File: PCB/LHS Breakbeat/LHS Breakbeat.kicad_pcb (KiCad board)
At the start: 2 copper layers, 114 x 61.4 mm, 47 parts, among them J1 Steppers In, J10 RGB, J11 Filament Sensor / Tach, J12 Endstop X, J13 Endstop Y, J14 Fan Aux, J15 Fan Part, J16 Fan Hotend/Can HL, J17 Motor X, J19 Motor X1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

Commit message: v1.01: changing copper weight to 2oz, adding xt30 cutout, various tolerance updates
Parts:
- moved TP1 0.20 mm to (160.7, 91.4)
- moved TP2 0.19 mm to (160.8, 94.8)
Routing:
- net /AGND: track 228.3 -> 268.7 mm
- net /X-B1: track 62.0 -> 64.9 mm
- net /X-B2: track 64.7 -> 67.6 mm
- net /Y1-A2: track 54.6 -> 52.3 mm
- net /PWM_HB: track 29.8 -> 28.1 mm
- net /X-A2: track 67.5 -> 66.2 mm
- net /X-A1: track 70.6 -> 69.6 mm
- net GND: track 24.3 -> 25.0 mm
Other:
- outline, holes or cut-outs redrawn
- board text added: "Circuit Limits:"
- board text added: "Gnd⏚"
- board text added: "Hotend Heater: 24V, 115W, 4.8A Bed Heater: 24V, 220W, 9.2A Fans: 24V, 2A RGB/5V: 2A Steppers: 2.7A"
- board text added: "RGB"
- board text added: "VOL 1.01"
- board text added: "⏚"
- board text removed: "Gnd"
- board text removed: "VOL 1"

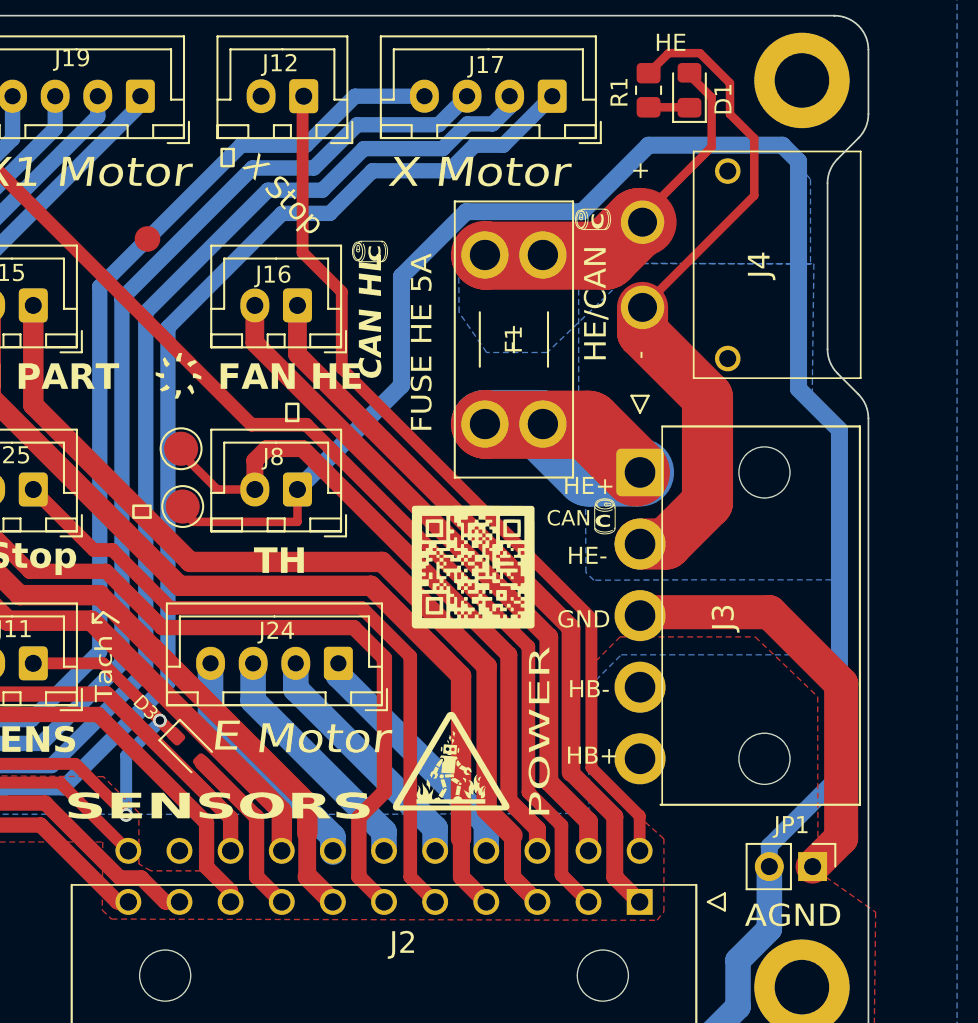
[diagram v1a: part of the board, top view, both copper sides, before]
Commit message: updating zone names
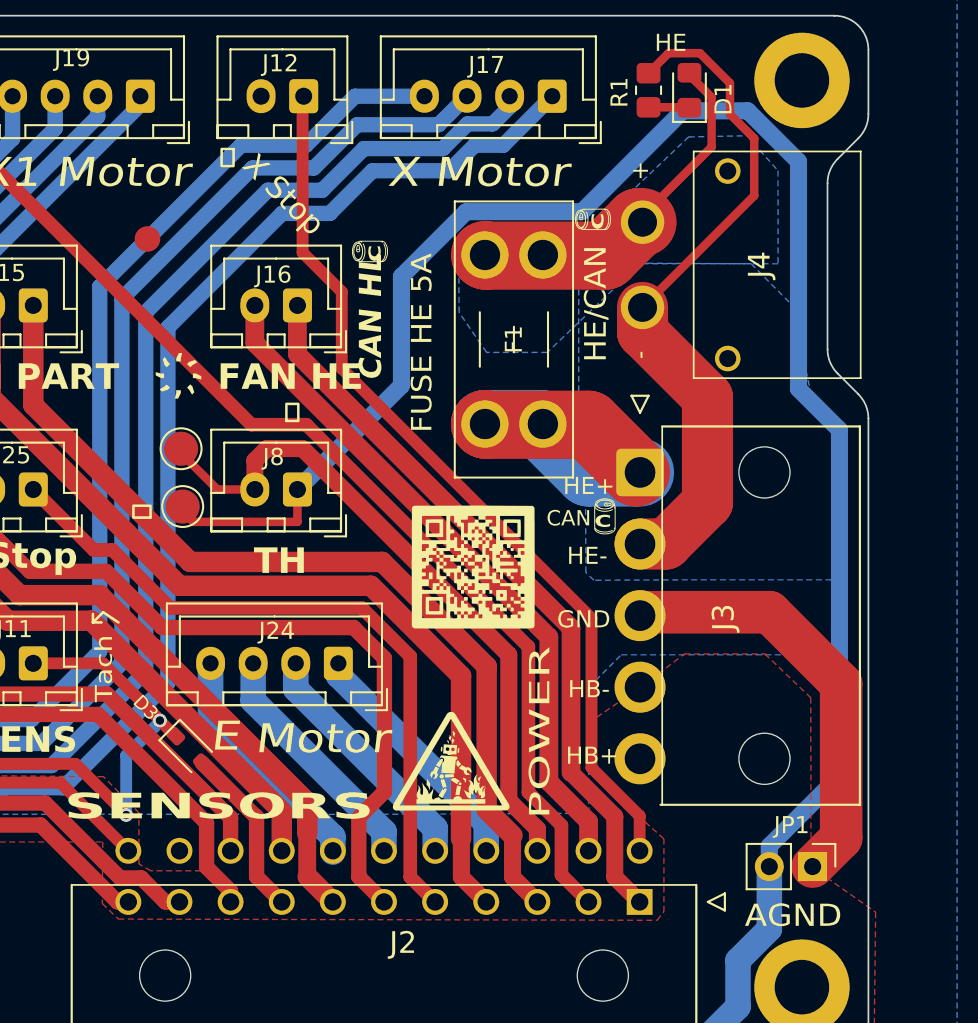
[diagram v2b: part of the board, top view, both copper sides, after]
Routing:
- net /AGND: track 268.7 -> 270.4 mm
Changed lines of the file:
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@@
     (effects (font (size 1 1) (thickness 0.15)))
   )
-  (segment (start 199.4 105.2) (end 199.4 114.25) (width 2) (layer "F.Cu") (net 1))
-  (segment (start 187.8 101) (end 195.2 101) (width 2) (layer "F.Cu") (net 1))
-  (segment (start 199.4 114.25) (end 197.725 115.925) (width 2) (layer "F.Cu") (net 1))
-  (segment (start 187.6 101.2) (end 187.8 101) (width 2) (layer "F.Cu") (net 1))
-  (segment (start 195.2 101) (end 199.4 105.2) (width 2) (layer "F.Cu") (net 1))
+  (segment (start 199.4 105.2) (end 199.4 114.25) (width 2.5) (layer "F.Cu") (net 1))
+  (segment (start 187.8 101) (end 195.2 101) (width 2.5) (layer "F.Cu") (net 1))
+  (segment (start 199.4 114.25) (end 197.725 115.925) (width 2.5) (layer "F.Cu") (net 1))
+  (segment (start 187.6 101.2) (end 187.8 101) (width 2.5) (layer "F.Cu") (net 1))
+  (segment (start 195.2 101) (end 199.4 105.2) (width 2.5) (layer "F.Cu") (net 1))
   (segment (start 190.475 71.375) (end 190.5 71.4) (width 0.25) (layer "F.Cu") (net 2))
   (segment (start 188.1 71.375) (end 190.475 71.375) (width 0.5) (layer "F.Cu") (net 2))
@@
   (segment (start 117.2 90.2) (end 119.1 92.1) (width 1) (layer "F.Cu") (net 10))
   (segment (start 97.2 100.1) (end 95.7 100.1) (width 0.8) (layer "F.Cu") (net 10))
+  (segment (start 177.4 77.5) (end 184.2 77.5) (width 1) (layer "B.Cu") (net 10))
+  (segment (start 196.9 74.56) (end 196.9 87.9) (width 1) (layer "B.Cu") (net 10))
+  (segment (start 193.35 121.425) (end 193.35 124.15) (width 1.5) (layer "B.Cu") (net 10))
   (segment (start 196.9 87.9) (end 199.3 90.3) (width 1) (layer "B.Cu") (net 10))
-  (segment (start 193.35 121.425) (end 193.35 124.15) (width 1.5) (layer "B.Cu") (net 10))
+  (segment (start 167.5 93.8) (end 173.6 87.7) (width 1) (layer "B.Cu") (net 10))
   (segment (start 193.35 124.15) (end 191.05 126.45) (width 1.5) (layer "B.Cu") (net 10))
-  (segment (start 199.3 110.607919) (end 195.185 114.722919) (width 1) (layer "B.Cu") (net 10))
+  (segment (start 184.2 77.5) (end 190.12 71.58) (width 1) (layer "B.Cu") (net 10))
   (segment (start 94.629364 112.229364) (end 94.629364 104.429364) (width 1.5) (layer "B.Cu") (net 10))
   (segment (start 191.05 126.45) (end 111.95 126.45) (width 1.5) (layer "B.Cu") (net 10))
-  (segment (start 167.5 93.8) (end 173.6 87.7) (width 1) (layer "B.Cu") (net 10))
   (segment (start 199.3 90.3) (end 199.3 110.607919) (width 1) (layer "B.Cu") (net 10))
+  (segment (start 173.6 87.7) (end 173.6 81.3) (width 1) (layer "B.Cu") (net 10))
+  (segment (start 193.92 71.58) (end 196.9 74.56) (width 1) (layer "B.Cu") (net 10))
   (segment (start 173.6 81.3) (end 177.4 77.5) (width 1) (layer "B.Cu") (net 10))
-  (segment (start 195.950252 73.6) (end 196.9 74.549748) (width 1) (layer "B.Cu") (net 10))
-  (segment (start 184.2 77.5) (end 188.1 73.6) (width 1) (layer "B.Cu") (net 10))
-  (segment (start 188.1 73.6) (end 195.950252 73.6) (width 1) (layer "B.Cu") (net 10))
-  (segment (start 196.9 74.549748) (end 196.9 87.9) (width 1) (layer "B.Cu") (net 10))
-  (segment (start 173.6 87.7) (end 173.6 81.3) (width 1) (layer "B.Cu") (net 10))
-  (segment (start 195.185 114.722919) (end 195.185 115.925) (width 1) (layer "B.Cu") (net 10))
-  (segment (start 177.4 77.5) (end 184.2 77.5) (width 1) (layer "B.Cu") (net 10))
   (segment (start 111.95 126.45) (end 110.5 125) (width 1.5) (layer "B.Cu") (net 10))
   (segment (start 110.5 125) (end 110.5 122.225) (width 1.5) (layer "B.Cu") (net 10))
+  (segment (start 190.12 71.58) (end 193.92 71.58) (width 1) (layer "B.Cu") (net 10))
+  (segment (start 195.185 114.722919) (end 195.185 115.925) (width 1) (layer "B.Cu") (net 10))
   (segment (start 106.075 117.8) (end 100.2 117.8) (width 1.5) (layer "B.Cu") (net 10))
   (segment (start 195.185 115.925) (end 195.185 119.59) (width 1.5) (layer "B.Cu") (net 10))
@@
   (segment (start 94.629364 104.429364) (end 93 102.8) (width 1.5) (layer "B.Cu") (net 10))
   (segment (start 100.2 117.8) (end 94.629364 112.229364) (width 1.5) (layer "B.Cu") (net 10))
+  (segment (start 199.3 110.607919) (end 195.185 114.722919) (width 1) (layer "B.Cu") (net 10))
   (segment (start 187.57825 112.954848) (end 184.75 110.126598) (width 0.7) (layer "F.Cu") (net 11))
   (segment (start 170.1 82.2) (end 167.8 79.9) (width 0.7) (layer "F.Cu") (net 11))
@@
   (segment (start 187.6 97) (end 189.120279 97) (width 3) (layer "F.Cu") (net 57))
   (segment (start 192.875 69.960051) (end 192.875 71.775) (width 0.5) (layer "F.Cu") (net 57))
-  (zone (net 5) (net_name "+5V") (layer "F.Cu") (name "PWM HB") (hatch edge 0.5)
+  (zone (net 5) (net_name "+5V") (layer "F.Cu") (name "+5V") (hatch edge 0.5)
     (connect_pads yes (clearance 0.4))
     (min_thickness 0.25) (filled_areas_thickness no)
@@
     )
   )
-  (zone (net 4) (net_name "/HB+") (layer "F.Cu") (name "PWM HB") (hatch edge 0.5)
+  (zone (net 4) (net_name "/HB+") (layer "F.Cu") (name "HB") (hatch edge 0.5)
     (priority 2)
     (connect_pads yes (clearance 0.4))
@@
         (xy 132.00504 114.48004)
         (xy 156.077557 114.482926)
-        (xy 156.046863 118.475733)
-        (xy 156.588861 119.005582)
+        (xy 156.04983 118.089842)
+        (xy 156.987474 119.006468)
         (xy 188.6 119.076813)
         (xy 189 118.575)
         (xy 189 114.3)
         (xy 184.6 110.325)
-        (xy 184.6 104.275)
-        (xy 186.425 102.45)
-        (xy 194.358338 102.45)
-        (xy 198.023468 105.953318)
-        (xy 198.040919 116.217331)
+        (xy 184.6 107.475)
+        (xy 187.785655 105.298155)
+        (xy 190.2 103.45)
+        (xy 194.930622 103.45)
+        (xy 197.616263 106.017073)
+        (xy 197.633118 115.930206)
         (xy 201.425 118.6)
         (xy 201.3 128.975)
@@
     )
   )
-  (zone (net 9) (net_name "/Fused HB") (layer "F.Cu") (name "PWM HB") (hatch edge 0.5)
+  (zone (net 9) (net_name "/Fused HB") (layer "F.Cu") (name "Fused HB") (hatch edge 0.5)
     (priority 3)
     (connect_pads yes (clearance 0.4))
@@
     )
   )
-  (zone (net 8) (net_name "/Fused HE") (layer "B.Cu") (name "PWM HB") (hatch edge 0.5)
+  (zone (net 0) (net_name "") (layer "B.Cu") (hatch edge 0.5)
+    (connect_pads (clearance 0))
+    (min_thickness 0.25) (filled_areas_thickness no)
+    (keepout (tracks allowed) (vias allowed) (pads allowed) (copperpour not_allowed) (footprints allowed))
+    (fill (thermal_gap 0.5) (thermal_bridge_width 0.5))
+    (polygon
+      (pts
+        (xy 196.656002 114.791466)
+        (xy 198.810084 114.791466)
+        (xy 198.810084 117.033727)
+        (xy 196.656002 117.033727)
+      )
+    )
+  )
+  (zone (net 8) (net_name "/Fused HE") (layer "B.Cu") (name "Fused HE") (hatch edge 0.5)
     (priority 6)
     (connect_pads yes (clearance 0.4))
@@
     (polygon
       (pts
-        (xy 195.880401 73.6)
-        (xy 197.6 75.6)
-        (xy 197.603371 80.568831)
+        (xy 193.868541 73.045829)
+        (xy 195.695127 75.094891)
+        (xy 195.698835 80.560467)
         (xy 187.623386 80.525)
         (xy 182.153683 85.76)
@@
         (xy 176.954074 79.161628)
         (xy 177.73992 78.397712)
-        (xy 183.843567 78.400389)
-        (xy 188.165792 73.426574)
+        (xy 184.9 78.400389)
+        (xy 190.45 73.113818)
       )
     )
@@
         (xy 184 80.925)
         (xy 184.375 80.55)
-        (xy 197.8 80.55)
+        (xy 194.114083 80.55)
+        (xy 196.507439 82.963464)
         (xy 197.7 88.5)
         (xy 199.4 90.5)
